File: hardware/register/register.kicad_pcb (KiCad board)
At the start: 4 copper layers, 99 x 60 mm, 91 parts, among them J1 Conn_02x04_Odd_Even, J2 Conn_02x04_Odd_Even, J3 Conn_02x04_Odd_Even, Q1 BS170, Q10 BS170, Q11 BS170, Q2 BS170, Q3 BS170, Q4 BS170, Q5 BS170, Q6 BS170, Q7 BS170, Q8 BS170, Q9 BS170, U1 74HC00, U10 74HC00, U11 74HC00, U12 74HC00, U13 74HC00, U14 74HC00, U15 74HC00, U16 74LS00, U17 74HC00, U18 74HC00, U19 74HC00, U2 74HC00, U20 74HC00, U21 74HC00, U22 74HC00, U23 74HC00, U24 74HC00, U25 74HC00, U3 74HC00, U4 74HC00, U5 74HC00, U6 74HC00, U7 74HC00, U8 74HC00, U9 74HC00

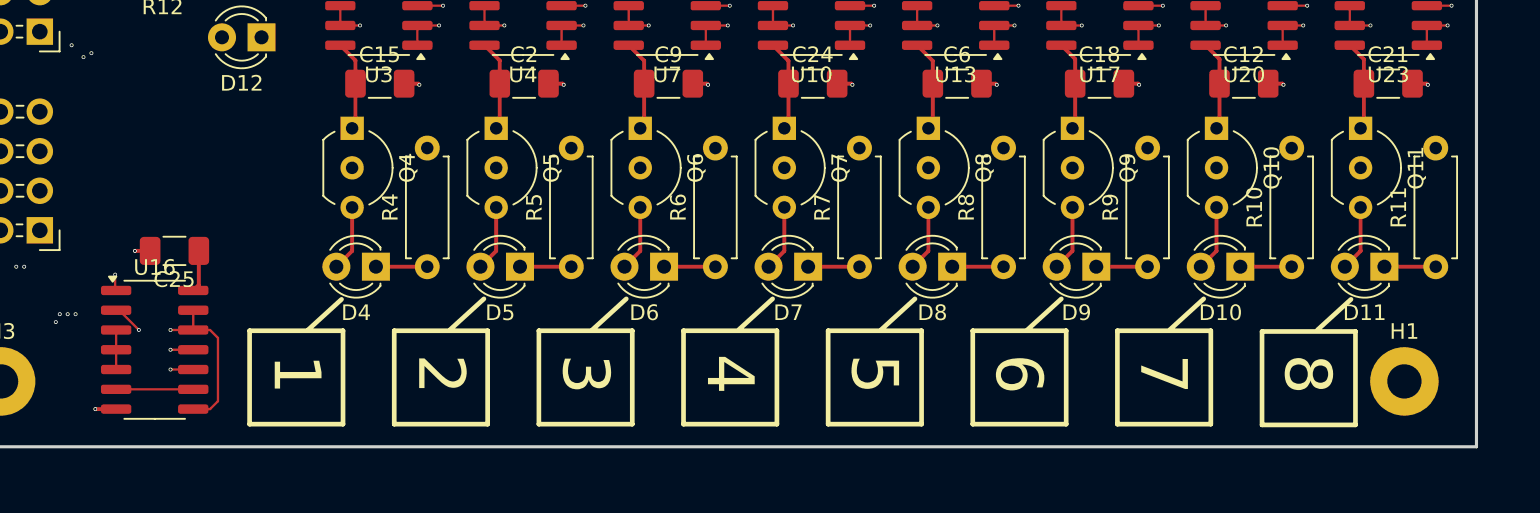
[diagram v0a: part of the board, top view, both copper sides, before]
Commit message: started CPU emulator software
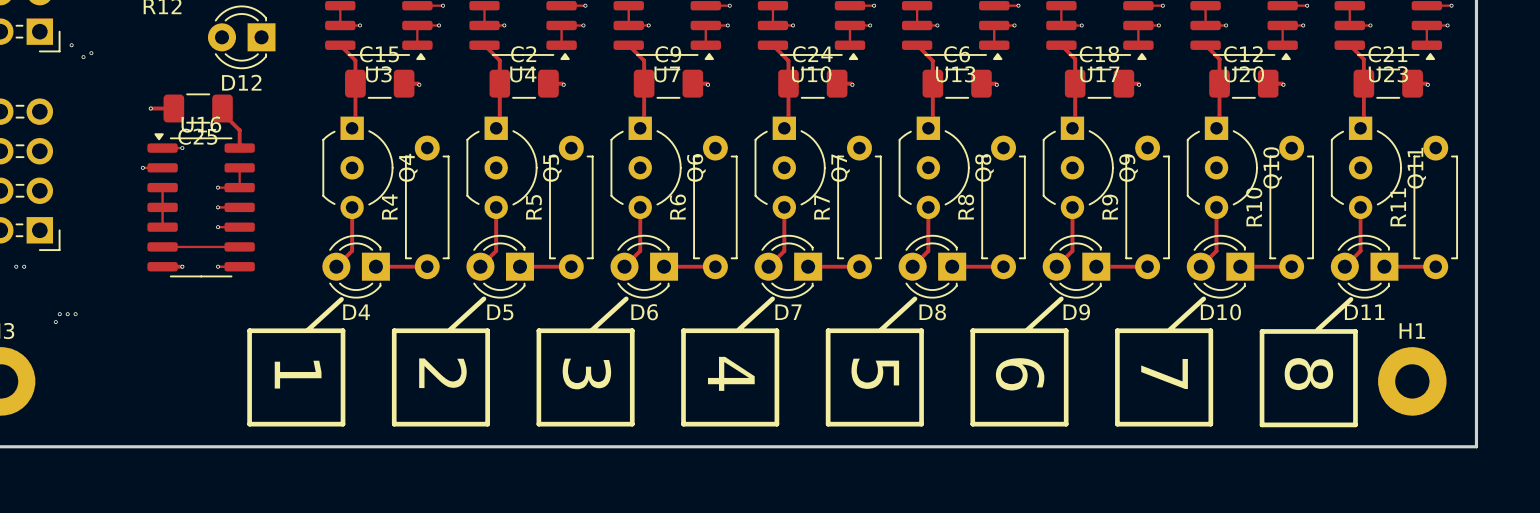
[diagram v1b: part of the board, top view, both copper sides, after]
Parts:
- moved U16 9.62 mm to (55.6, -75.2)
- moved C25 9.27 mm to (55.4, -81.5)
- moved H1 0.51 mm to (133.4, -64.0)
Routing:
- net Net-(J1-Pin_1): track 36.5 -> 25.5 mm
- net Net-(Q1-G): track 56.1 -> 47.3 mm, vias 1 -> 2
- net Net-(J1-Pin_4): track 44.8 -> 36.4 mm
- net Net-(Q2-G): track 39.5 -> 31.6 mm
- net Net-(J1-Pin_3): track 39.1 -> 34.6 mm
- net +5V: track 263.7 -> 264.3 mm

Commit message: redesigned register PCB with SMD components
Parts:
- removed H1: MountingHole_Pad, MountingHole:MountingHole_2.2mm_M2_Pad
- added Q12: IRLML6244, Package_TO_SOT_SMD:SOT-23_Handsoldering, F.Cu at (90.2, 102.1)
- added Q13: IRLML6244, Package_TO_SOT_SMD:SOT-23_Handsoldering, F.Cu at (80.6, 83.0)
- added Q14: IRLML6244, Package_TO_SOT_SMD:SOT-23_Handsoldering, F.Cu at (80.6, 89.6)
- added R13: 400, Resistor_SMD:R_1206_3216Metric_Pad1.30x1.75mm_HandSolder, F.Cu at (86.9, 76.5)
- added R14: 400, Resistor_SMD:R_1206_3216Metric_Pad1.30x1.75mm_HandSolder, F.Cu at (86.9, 83.1)
- added R15: 400, Resistor_SMD:R_1206_3216Metric_Pad1.30x1.75mm_HandSolder, F.Cu at (86.9, 89.7)
- D1, D10, D11, D12, D2, D3, D4, D5, D6, D7, D8, D9: footprint LED_THT:LED_D3.0mm -> LED_SMD:LED_1206_3216Metric_Pad1.42x1.75mm_HandSolder
- Q1, Q10, Q11, Q2, Q3, Q4, Q5, Q6, Q7, Q8, Q9: value BS170 -> IRLML6244; footprint Package_TO_SOT_THT:TO-92_Inline_Wide -> Package_TO_SOT_SMD:SOT-23_Handsoldering
- R1, R10, R11, R12, R2, R3, R4, R5, R6, R7, R8, R9: value 200 -> 400; footprint Resistor_THT:R_Axial_DIN0207_L6.3mm_D2.5mm_P7.62mm_Horizontal -> Resistor_SMD:R_1206_3216Metric_Pad1.30x1.75mm_HandSolder
- moved R1 225.2 mm to (90.2, 105.7), turned to 0 degrees
- moved Q1 225.1 mm to (90.2, 109.1)
- moved R2 223.3 mm to (90.2, 112.6), turned to 0 degrees
- moved Q2 223.2 mm to (90.2, 116.1)
- moved R3 221.5 mm to (90.2, 119.6), turned to 0 degrees
- moved Q3 213.8 mm to (99.6, 113.3)
- moved Q10 198.4 mm to (164.4, 113.3), turned to 0 degrees
- moved Q4 198.4 mm to (108.9, 113.3), turned to 0 degrees
- moved Q5 198.4 mm to (118.2, 113.3), turned to 0 degrees
- moved Q6 198.4 mm to (127.4, 113.3), turned to 0 degrees
- moved Q7 198.4 mm to (136.7, 113.3), turned to 0 degrees
- moved Q8 198.4 mm to (145.9, 113.3), turned to 0 degrees
- moved Q9 198.4 mm to (155.2, 113.3), turned to 0 degrees
- moved C25 197.4 mm to (83.1, 113.9), turned to 0 degrees
- moved C1 195.2 mm to (153.5, 97.2)
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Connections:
- net Net-(J1-Pin_1) renamed /WEN
- J1 pad 3: Net-(J1-Pin_3) -> /!CLR
- J1 pad 4: Net-(J1-Pin_4) -> /CLK
- Q1 pad 1: +5V -> Net-(Q1-G)
- Q1 pad 2: Net-(Q1-G) -> Net-(Q1-S)
- Q1 pad 3: Net-(D1-A) -> +5V
- Q10 pad 1: +5V -> Net-(Q10-G)
- Q10 pad 2: Net-(Q10-G) -> Net-(D11-A)
- Q10 pad 3: Net-(D10-A) -> +5V
- Q11 pad 1: +5V -> /CLK
- Q11 pad 2: Net-(Q11-G) -> Net-(D1-A)
- Q11 pad 3: Net-(D11-A) -> +5V
- Q2 pad 1: +5V -> /!CLR
- Q2 pad 2: Net-(Q2-G) -> Net-(Q2-S)
- Q2 pad 3: Net-(D2-A) -> +5V
- Q3 pad 1: +5V -> Net-(Q3-G)
- Q3 pad 2: Net-(J1-Pin_3) -> Net-(D4-A)
- Q3 pad 3: Net-(D3-A) -> +5V
- Q4 pad 1: +5V -> Net-(Q4-G)
- Q4 pad 2: Net-(Q4-G) -> Net-(D5-A)
- Q4 pad 3: Net-(D4-A) -> +5V
- Q5 pad 1: +5V -> Net-(Q5-G)
- Q5 pad 2: Net-(Q5-G) -> Net-(D6-A)
- Q5 pad 3: Net-(D5-A) -> +5V
- Q6 pad 1: +5V -> Net-(Q6-G)
- Q6 pad 2: Net-(Q6-G) -> Net-(D7-A)
- Q6 pad 3: Net-(D6-A) -> +5V
- Q7 pad 1: +5V -> Net-(Q7-G)
- Q7 pad 2: Net-(Q7-G) -> Net-(D8-A)
- Q7 pad 3: Net-(D7-A) -> +5V
- Q8 pad 1: +5V -> Net-(Q8-G)
- Q8 pad 2: Net-(Q8-G) -> Net-(D9-A)
- Q8 pad 3: Net-(D8-A) -> +5V
- Q9 pad 1: +5V -> Net-(Q9-G)
- Q9 pad 2: Net-(Q9-G) -> Net-(D10-A)
- Q9 pad 3: Net-(D9-A) -> +5V
- R1 pad 1: Net-(D1-K) -> Net-(Q12-S)
- R2 pad 1: Net-(D2-K) -> Net-(Q1-S)
- R3 pad 1: Net-(D3-K) -> Net-(Q2-S)
- U1 pad 11: Net-(Q4-G) -> Net-(Q3-G)
- U1 pad 2: Net-(D1-A) -> Net-(Q12-S)
- U1 pad 9: Net-(D2-A) -> Net-(Q1-S)
- U10 pad 5: Net-(D3-A) -> Net-(Q2-S)
- U11 pad 11: Net-(Q7-G) -> Net-(Q6-G)
- U11 pad 2: Net-(D1-A) -> Net-(Q12-S)
- U11 pad 9: Net-(D2-A) -> Net-(Q1-S)
- U12 pad 1: Net-(D1-A) -> Net-(Q12-S)
- U12 pad 10: Net-(D2-A) -> Net-(Q1-S)
- U12 pad 12: Net-(Q7-G) -> Net-(Q6-G)
- U13 pad 5: Net-(D3-A) -> Net-(Q2-S)
- U14 pad 11: Net-(Q8-G) -> Net-(Q7-G)
- U14 pad 2: Net-(D1-A) -> Net-(Q12-S)
- U14 pad 9: Net-(D2-A) -> Net-(Q1-S)
- U15 pad 1: Net-(D1-A) -> Net-(Q12-S)
- U15 pad 10: Net-(D2-A) -> Net-(Q1-S)
- U15 pad 12: Net-(Q8-G) -> Net-(Q7-G)
- U16 pad 1: Net-(J1-Pin_3) -> /!CLR
- U16 pad 10: Net-(J1-Pin_4) -> /CLK
- U16 pad 11: Net-(Q2-G) -> Net-(Q1-G)
- U16 pad 12: Net-(Q1-G) -> Net-(Q12-G)
- U16 pad 13: Net-(Q1-G) -> Net-(Q12-G)
- U16 pad 8: Net-(Q1-G) -> Net-(Q12-G)
- U17 pad 5: Net-(D3-A) -> Net-(Q2-S)
- U18 pad 11: Net-(Q9-G) -> Net-(Q8-G)
- U18 pad 2: Net-(D1-A) -> Net-(Q12-S)
- U18 pad 9: Net-(D2-A) -> Net-(Q1-S)
- U19 pad 1: Net-(D1-A) -> Net-(Q12-S)
- U19 pad 10: Net-(D2-A) -> Net-(Q1-S)
- U19 pad 12: Net-(Q9-G) -> Net-(Q8-G)
- U2 pad 1: Net-(D1-A) -> Net-(Q12-S)
- U2 pad 10: Net-(D2-A) -> Net-(Q1-S)
- U2 pad 12: Net-(Q4-G) -> Net-(Q3-G)
- U20 pad 5: Net-(D3-A) -> Net-(Q2-S)
- U21 pad 11: Net-(Q10-G) -> Net-(Q9-G)
- U21 pad 2: Net-(D1-A) -> Net-(Q12-S)
- U21 pad 9: Net-(D2-A) -> Net-(Q1-S)
- U22 pad 1: Net-(D1-A) -> Net-(Q12-S)
- U22 pad 10: Net-(D2-A) -> Net-(Q1-S)
- U22 pad 12: Net-(Q10-G) -> Net-(Q9-G)
- U23 pad 5: Net-(D3-A) -> Net-(Q2-S)
- U24 pad 11: Net-(Q11-G) -> Net-(Q10-G)
- U24 pad 2: Net-(D1-A) -> Net-(Q12-S)
- U24 pad 9: Net-(D2-A) -> Net-(Q1-S)
- U25 pad 1: Net-(D1-A) -> Net-(Q12-S)
- U25 pad 10: Net-(D2-A) -> Net-(Q1-S)
- U25 pad 12: Net-(Q11-G) -> Net-(Q10-G)
- U3 pad 5: Net-(D3-A) -> Net-(Q2-S)
- U4 pad 5: Net-(D3-A) -> Net-(Q2-S)
- U5 pad 11: Net-(Q5-G) -> Net-(Q4-G)
- U5 pad 2: Net-(D1-A) -> Net-(Q12-S)
- U5 pad 9: Net-(D2-A) -> Net-(Q1-S)
- U6 pad 1: Net-(D1-A) -> Net-(Q12-S)
- U6 pad 10: Net-(D2-A) -> Net-(Q1-S)
- U6 pad 12: Net-(Q5-G) -> Net-(Q4-G)
- U7 pad 5: Net-(D3-A) -> Net-(Q2-S)
- U8 pad 11: Net-(Q6-G) -> Net-(Q5-G)
- U8 pad 2: Net-(D1-A) -> Net-(Q12-S)
- U8 pad 9: Net-(D2-A) -> Net-(Q1-S)
- U9 pad 1: Net-(D1-A) -> Net-(Q12-S)
- U9 pad 10: Net-(D2-A) -> Net-(Q1-S)
- U9 pad 12: Net-(Q6-G) -> Net-(Q5-G)
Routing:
- net Net-(Q1-S): track 0.00 -> 202.7 mm, vias 0 -> 20
- net Net-(Q12-S): track 0.00 -> 195.5 mm, vias 0 -> 20
- net Net-(D1-A): track 189.4 -> 2.61 mm, vias 18 -> 0
- net Net-(D2-A): track 182.6 -> 2.61 mm, vias 18 -> 0
- net +5V: track 264.3 -> 428.8 mm
- net Net-(Q2-S): track 0.00 -> 105.6 mm, vias 0 -> 10
- net Net-(D3-A): track 93.7 -> 2.61 mm, vias 8 -> 0
- net Net-(Q3-G): track 0.00 -> 41.7 mm, vias 0 -> 3
- net Net-(Q11-G): track 41.4 -> 0.00 mm, vias 2 -> 0
- net /!CLR: track 0.00 -> 39.3 mm, vias 0 -> 4
- net Net-(Q1-G): track 47.3 -> 8.54 mm
- net /CLK: track 0.00 -> 38.0 mm, vias 0 -> 2
- net Net-(J1-Pin_4): track 36.4 -> 0.00 mm, vias 1 -> 0
- net Net-(J1-Pin_3): track 34.6 -> 0.00 mm, vias 2 -> 0
- net Net-(Q2-G): track 31.6 -> 0.00 mm, vias 1 -> 0
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- added copper zone on In1.Cu, net GND
- added copper zone on In2.Cu, net GND
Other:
- board size 99 x 60 mm -> 99 x 50 mm
- board text added: "CLK"
- board text added: "CLR"
- board text added: "PWR"
- board text added: "WEN"

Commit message: generated production files, including BOM and POS
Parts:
- added TP1: TestPoint, TestPoint:TestPoint_Pad_D2.0mm, B.Cu at (99.7, 103.6)
- added TP10: TestPoint, TestPoint:TestPoint_Pad_D2.0mm, B.Cu at (109.4, 112.0)
- added TP11: TestPoint, TestPoint:TestPoint_Pad_D2.0mm, B.Cu at (118.5, 112.0)
- added TP12: TestPoint, TestPoint:TestPoint_Pad_D2.0mm, B.Cu at (127.6, 112.0)
- added TP13: TestPoint, TestPoint:TestPoint_Pad_D2.0mm, B.Cu at (136.6, 112.0)
- added TP14: TestPoint, TestPoint:TestPoint_Pad_D2.0mm, B.Cu at (145.7, 112.0)
- added TP15: TestPoint, TestPoint:TestPoint_Pad_D2.0mm, B.Cu at (154.8, 112.0)
- added TP16: TestPoint, TestPoint:TestPoint_Pad_D2.0mm, B.Cu at (164.4, 112.0)
- added TP17: TestPoint, TestPoint:TestPoint_Pad_D2.0mm, B.Cu at (97.4, 84.3)
- added TP18: TestPoint, TestPoint:TestPoint_Pad_D2.0mm, B.Cu at (106.9, 84.3)
- added TP19: TestPoint, TestPoint:TestPoint_Pad_D2.0mm, B.Cu at (116.5, 84.3)
- added TP2: TestPoint, TestPoint:TestPoint_Pad_D2.0mm, B.Cu at (109.2, 103.6)
- added TP20: TestPoint, TestPoint:TestPoint_Pad_D2.0mm, B.Cu at (126.1, 84.3)
- added TP21: TestPoint, TestPoint:TestPoint_Pad_D2.0mm, B.Cu at (135.1, 84.3)
- added TP22: TestPoint, TestPoint:TestPoint_Pad_D2.0mm, B.Cu at (144.2, 84.3)
- added TP23: TestPoint, TestPoint:TestPoint_Pad_D2.0mm, B.Cu at (153.3, 84.3)
- added TP24: TestPoint, TestPoint:TestPoint_Pad_D2.0mm, B.Cu at (162.8, 84.3)
- added TP25: TestPoint, TestPoint:TestPoint_Pad_D2.0mm, B.Cu at (94.3, 109.0)
- added TP26: TestPoint, TestPoint:TestPoint_Pad_D2.0mm, B.Cu at (94.3, 104.9)
- added TP27: TestPoint, TestPoint:TestPoint_Pad_D2.0mm, B.Cu at (94.3, 100.9)
- added TP3: TestPoint, TestPoint:TestPoint_Pad_D2.0mm, B.Cu at (118.1, 103.6)
- added TP4: TestPoint, TestPoint:TestPoint_Pad_D2.0mm, B.Cu at (127.1, 103.6)
- added TP5: TestPoint, TestPoint:TestPoint_Pad_D2.0mm, B.Cu at (136.7, 103.6)
- added TP6: TestPoint, TestPoint:TestPoint_Pad_D2.0mm, B.Cu at (145.8, 103.6)
- added TP7: TestPoint, TestPoint:TestPoint_Pad_D2.0mm, B.Cu at (155.2, 103.6)
- added TP8: TestPoint, TestPoint:TestPoint_Pad_D2.0mm, B.Cu at (164.5, 103.6)
- added TP9: TestPoint, TestPoint:TestPoint_Pad_D2.0mm, B.Cu at (99.8, 112.0)
- R1, R2, R3: value 400 -> 1000
- R10, R11, R12, R13, R14, R15, R4, R5, R6, R7, R8, R9: value 400 -> 100
- U16: value 74LS00 -> 74HC00
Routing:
- net Net-(Q1-S): track 202.7 -> 211.9 mm
- net Net-(TP17-Pad1): track 22.9 -> 29.9 mm
- net Net-(TP23-Pad1): track 22.8 -> 29.7 mm
- net Net-(TP18-Pad1): track 22.9 -> 29.8 mm
- net Net-(TP22-Pad1): track 22.8 -> 29.7 mm
- net Net-(TP24-Pad1): track 22.8 -> 29.6 mm
- net Net-(TP19-Pad1): track 22.8 -> 29.6 mm
- net Net-(TP21-Pad1): track 22.7 -> 29.5 mm
- net Net-(Q2-S): track 105.6 -> 112.3 mm
- net Net-(TP20-Pad1): track 22.8 -> 29.5 mm
- net Net-(Q4-G): track 41.7 -> 47.3 mm
- net Net-(Q5-G): track 41.8 -> 47.3 mm
- net Net-(Q6-G): track 41.7 -> 46.8 mm
- net Net-(Q3-G): track 41.7 -> 46.8 mm
- net Net-(Q7-G): track 41.9 -> 47.0 mm
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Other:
- board text added: "8 Bit Register | Rev A"
- board text added: "CONTROL"
- board text added: "D0"
- board text added: "D1"
- board text added: "D2"
- board text added: "D3"
- board text added: "D4"
- board text added: "D5"
- board text added: "D6"
- board text added: "D7"
- board text added: "GND"
- board text added: "READ"
- board text added: "VDD"
- board text added: "WRITE"

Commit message: redesigned register using SMD components
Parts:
- removed H2: MountingHole_Pad, MountingHole:MountingHole_2.2mm_M2_Pad
- removed J1, J2, J3: Conn_02x04_Odd_Even, Connector_PinHeader_2.54mm:PinHeader_2x04_P2.54mm_Horizontal
- added C26: 10uF, Capacitor_SMD:C_0603_1608Metric_Pad1.08x0.95mm_HandSolder, F.Cu at (91.2, 83.8)
- added C27: 10uF, Capacitor_SMD:C_0603_1608Metric_Pad1.08x0.95mm_HandSolder, F.Cu at (92.7, 83.8)
- added J4: Conn_02x16_Odd_Even, Connector_PinHeader_2.54mm:PinHeader_2x16_P2.54mm_Horizontal, F.Cu at (76.0, 116.8)
- C1, C10, C11, C12, C13, C14, C15, C16, C17, C18, C19, C2, C20, C21, C22, C23, C24, C25, C3, C4, C5, C6, C7, C8, C9: value 100nF -> 330nF; footprint Capacitor_SMD:C_1206_3216Metric_Pad1.33x1.80mm_HandSolder -> Capacitor_SMD:C_0603_1608Metric_Pad1.08x0.95mm_HandSolder
- D1, D10, D11, D12, D2, D3, D4, D5, D6, D7, D8, D9: footprint LED_SMD:LED_1206_3216Metric_Pad1.42x1.75mm_HandSolder -> LED_SMD:LED_0603_1608Metric_Pad1.05x0.95mm_HandSolder
- R1, R2, R3: footprint Resistor_SMD:R_1206_3216Metric_Pad1.30x1.75mm_HandSolder -> Resistor_SMD:R_0603_1608Metric_Pad0.98x0.95mm_HandSolder
- R10, R11, R12, R13, R14, R15, R4, R5, R6, R7, R8, R9: value 100 -> 1000; footprint Resistor_SMD:R_1206_3216Metric_Pad1.30x1.75mm_HandSolder -> Resistor_SMD:R_0603_1608Metric_Pad0.98x0.95mm_HandSolder
- moved H3 90.3 mm to (164.9, 119.1)
- moved R11 4.72 mm to (160.3, 117.3)
- moved R6 4.72 mm to (114.0, 117.3)
- moved R8 4.72 mm to (132.5, 117.3)
- moved R9 4.72 mm to (141.8, 117.3)
- moved R4 4.72 mm to (95.5, 117.3)
- moved R5 4.72 mm to (104.8, 117.3)
- moved R7 4.72 mm to (123.3, 117.3)
- moved R10 4.72 mm to (151.0, 117.3)
- moved D10 4.23 mm to (151.0, 115.8)
- moved D11 4.23 mm to (160.3, 115.8)
- moved D9 4.23 mm to (141.8, 115.8)
- moved D4 4.23 mm to (95.5, 115.8)
- moved D5 4.23 mm to (104.8, 115.8)
- moved D6 4.23 mm to (114.0, 115.8)
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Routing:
- net +5V: track 430.4 -> 500.7 mm, vias 0 -> 3
- net GND: track 104.9 -> 135.4 mm, vias 73 -> 363
- net /!CLR: track 39.3 -> 44.4 mm
- net /CLK: track 38.0 -> 33.1 mm, vias 2 -> 1
- net Net-(Q12-S): track 200.3 -> 202.6 mm
- net Net-(Q1-S): track 211.9 -> 214.1 mm
- net /WEN: track 33.6 -> 35.1 mm, vias 4 -> 3
- net Net-(Q3-G): track 46.8 -> 45.4 mm
- net Net-(Q5-G): track 47.3 -> 45.9 mm
- net Net-(D11-K): track 2.91 -> 1.53 mm
- net Net-(Q9-G): track 46.3 -> 45.0 mm
- net Net-(D12-K): track 2.82 -> 1.50 mm
- net Net-(D1-K): track 2.82 -> 1.50 mm
- net Net-(D2-K): track 2.82 -> 1.50 mm
- net Net-(D3-K): track 2.81 -> 1.50 mm
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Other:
- board text added: "0"
- board text added: "DI0"
- board text added: "DI1"
- board text added: "DI2"
- board text added: "DI3"
- board text added: "DI4"
- board text added: "DI5"
- board text added: "DI6"
- board text added: "DI7"
- board text added: "DO0"
- board text added: "DO1"
- board text added: "DO2"
- board text added: "DO3"
- board text added: "DO4"
- board text added: "DO5"
- board text added: "DO6"
- board text added: "DO7"
- board text added: "mrab"
- board text removed: "8"
- board text removed: "D0"
- board text removed: "D1"
- board text removed: "D2"
- board text removed: "D3"
- board text removed: "D4"
- board text removed: "D5"
- board text removed: "D6"
- board text removed: "D7"
